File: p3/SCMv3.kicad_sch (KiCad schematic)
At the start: 122 parts, among them IC1 40106, IC2 40106, IC3 TL082, J1 ISP, J1-OUT8 JACK-MONO-SWB, J2 Conn_01x02, J2-OUT7 JACK-MONO-SWB, J3 POWER, J3-OUT6 JACK-MONO-SWB, J4-OUT5 JACK-MONO-SWB, J5-OUT4 JACK-MONO-SWB, J6-OUT3 JACK-MONO-SWB, J7-OUT2 JACK-MONO-SWB, J8-OUT1 JACK-MONO-SWB, J9-CLK_IN1 JCLK_IN, Q1 Si2318, Q2 Si2318, Q3 Si2318, Q4 Si2318, U1 ATMEGA328-AU, Y1 16MHz_18pF_FA238

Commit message: p3 ready to connect pins: then route
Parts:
- removed J1: ISP, 4ms_Connector:Pins_2x03_2.54mm_TH, symbol 4ms_Connector:Conn_02x03
- removed U1: ATMEGA328-AU, 4ms_Package_QFP:TQFP-32_7x7mm_P0.8mm, symbol 4ms_IC:ATMEGA328-AU
- added C18, C22, C23: 0.1uF_0603_16V, 4ms_Capacitor:C_0603, symbol 4ms_Capacitor:0.1uF_0603_16V
- added C21: 10uF_0603_10V, 4ms_Capacitor:C_0603, symbol 4ms_Capacitor:10uF_0603_10V
- added J1: Conn_01x06, 4ms_Connector:Pins_1x06_2.54mm_TH_SWD, symbol 4ms_Connector:Conn_01x06
- added U2: AP7384-33, 4ms_Package_SOT:SOT23-3_PO132, symbol 4ms_Regulator:AP7384-33
- gave numbers to parts that had none: 2
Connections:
- net +12V: now also C18.1, C22.1, C23.1, U2.1 (VI)
- net +3.3VA: now also C21.1, U2.2 (VO)
- net +3V3: now also R16.2, J1.1 (Pin_1)
- net +5V: no longer C15.1, R16.2
- net -12VA: now also C15.1
- net GND: now also C18.2, C21.2, C22.2, C23.2, J1.3 (Pin_3), U2.3 (GND)
- net RESET: now also U1.4 (NRST), J1.5 (Pin_5)
- net CLKBUS_PWRHDR: now reaches J2.2 (Pin_2), J3.1 (P1), J3.2 (P2)
- net at C5.1, Y1.2: now also U1.2 (PF0)
- net at C4.1, Y1.1: now also U1.3 (PF1)
- net SWDIO: now reaches U1.23 (PA13)
- net SWDIO: now also J1.4 (Pin_4)
- net SWCLK: now reaches U1.24 (PA14)
- net SWCLK: now also J1.2 (Pin_2)
- net UC_OUT4_MOSI renamed UC_OUT4
- net UC_OUT5_MISO renamed UC_OUT5
- net UC_OUT6_SCK renamed UC_OUT6
- no-connect marks 43 -> 40
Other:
- note added: "ADC"
- note added: "CLKBUS->IN Jumper"
- note added: "Connect to an ADC pin:"
- note added: "Connect to any available pin:"
- note added: "FREERUN Jumper"
- note added: "LED Brightness Trimpot"
- moved on the sheet: C12, C13, C14, C16, C17, C19, C20, C4, C5, D10, D11, IC1G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

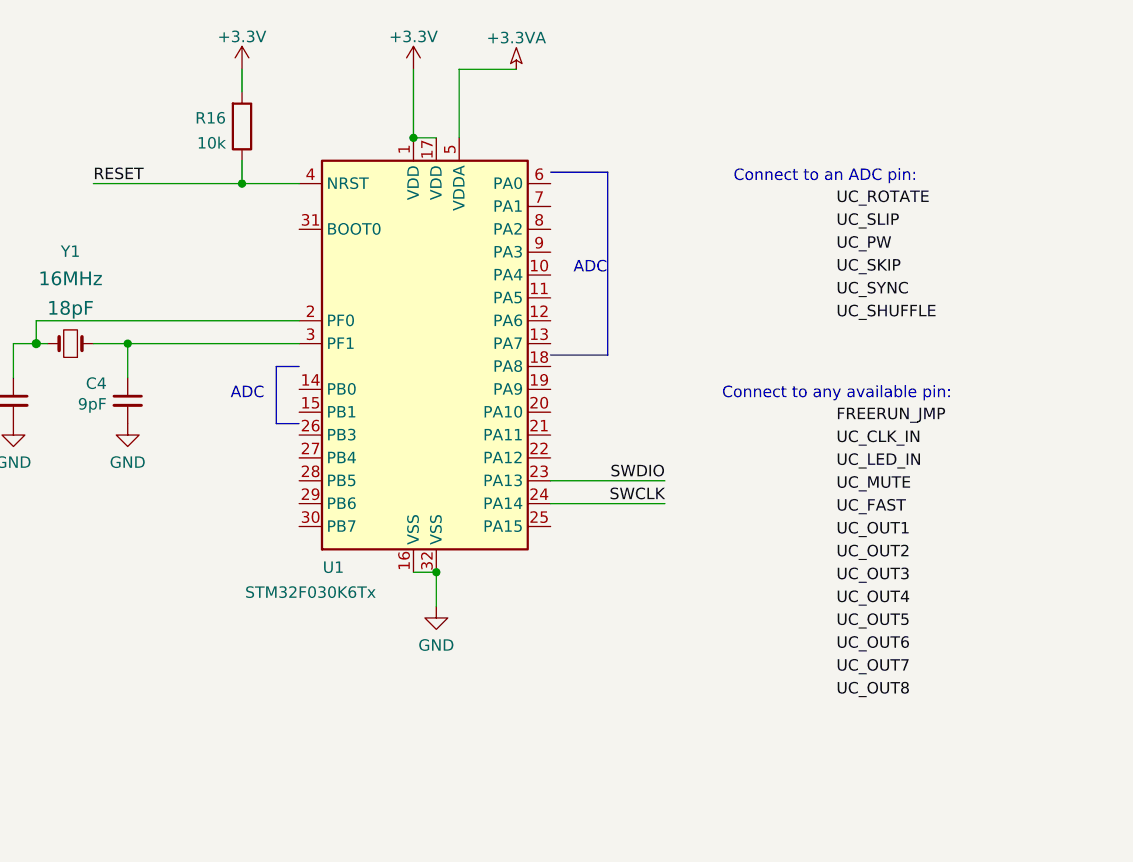
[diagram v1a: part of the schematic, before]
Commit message: Atmega replacement and other mods
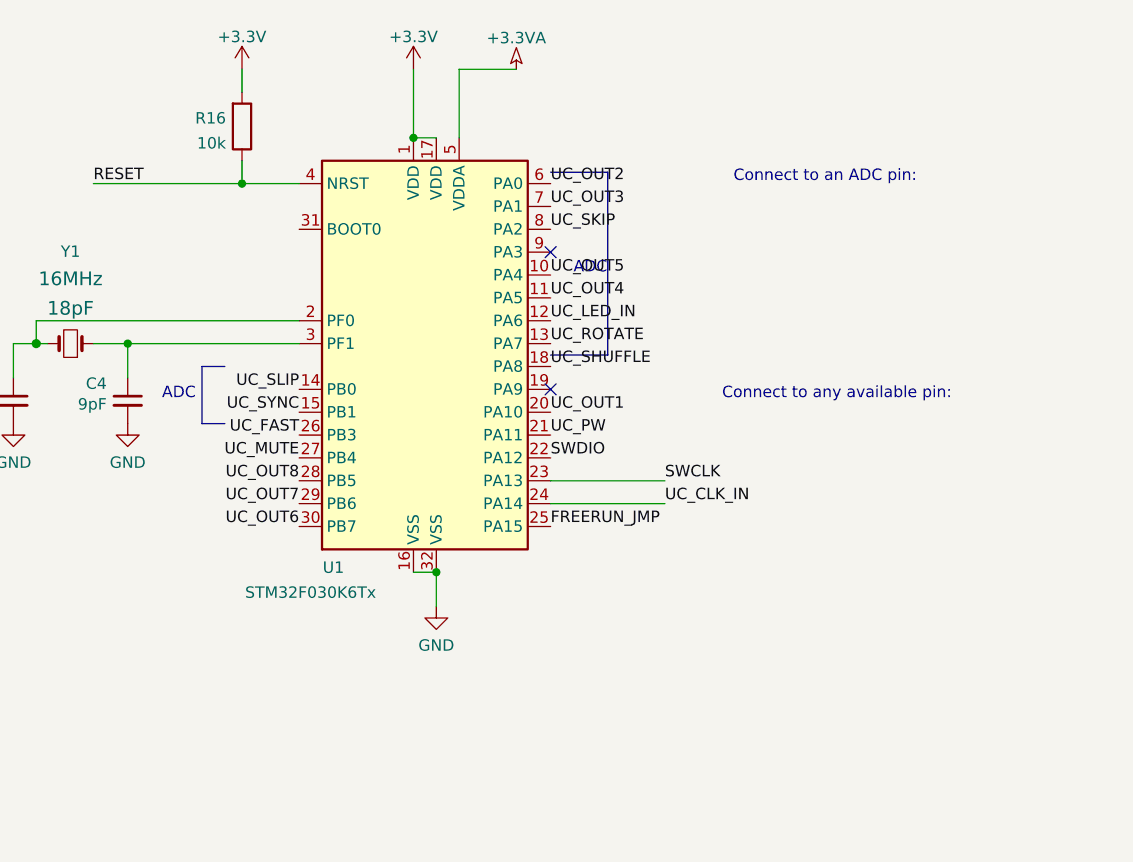
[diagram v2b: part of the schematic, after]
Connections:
- net FREERUN_JMP: now also U1.25 (PA15)
- net SWCLK: now also U1.23 (PA13); no longer U1.24 (PA14)
- net SWDIO: now also U1.22 (PA12); no longer U1.23 (PA13)
- net UC_CLK_IN: now also U1.24 (PA14)
- net UC_FAST: now also U1.26 (PB3)
- net UC_LED_IN: now also U1.12 (PA6)
- net UC_MUTE: now also U1.27 (PB4)
- net UC_OUT1: now also U1.20 (PA10)
- net UC_OUT2: now also U1.6 (PA0)
- net UC_OUT3: now also U1.7 (PA1)
- net UC_OUT4: now also U1.11 (PA5)
- net UC_OUT5: now also U1.10 (PA4)
- net UC_OUT6: now also U1.30 (PB7)
- net UC_OUT7: now also U1.29 (PB6)
- net UC_OUT8: now also U1.28 (PB5)
- net UC_PW: now also U1.21 (PA11)
- net UC_ROTATE: now also U1.13 (PA7)
- net UC_SHUFFLE: now also U1.18 (PA8)
- net UC_SKIP: now also U1.8 (PA2)
- net UC_SLIP: now also U1.14 (PB0)
- net UC_SYNC: now also U1.15 (PB1)
- no-connect marks 40 -> 42
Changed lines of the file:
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@@
   (no_connect (at 44.45 353.06))
   (no_connect (at 63.5 44.45))
+  (no_connect (at 91.44 111.76))
+  (no_connect (at 91.44 127))
   (no_connect (at 185.42 49.53))
   (no_connect (at 185.42 54.61))
@@
     (stroke (width 0) (type solid) (color 0 0 0 0))
   )
-  (polyline (pts (xy 60.96 124.46) (xy 60.96 130.81))
-    (stroke (width 0) (type default) (color 0 0 0 0))
-  )
-  (polyline (pts (xy 60.96 130.81) (xy 63.5 130.81))
-    (stroke (width 0) (type default) (color 0 0 0 0))
-  )
-  (polyline (pts (xy 63.5 124.46) (xy 60.96 124.46))
+  (polyline (pts (xy 52.705 124.46) (xy 52.705 130.81))
+    (stroke (width 0) (type default) (color 0 0 0 0))
+  )
+  (polyline (pts (xy 52.705 130.81) (xy 55.245 130.81))
+    (stroke (width 0) (type default) (color 0 0 0 0))
+  )
+  (polyline (pts (xy 55.245 124.46) (xy 52.705 124.46))
     (stroke (width 0) (type default) (color 0 0 0 0))
   )
@@
     (effects (font (size 2.54 2.54)) (justify left bottom))
   )
+  (text "ADC" (at 48.26 128.27 0)
+    (effects (font (size 1.27 1.27)) (justify left bottom))
+  )
   (text "FREERUN Jumper" (at 53.34 256.54 0)
     (effects (font (size 2.54 2.54)) (justify left bottom))
   )
-  (text "ADC" (at 55.88 128.27 0)
-    (effects (font (size 1.27 1.27)) (justify left bottom))
-  )
   (text "ADC" (at 93.98 114.3 0)
     (effects (font (size 1.27 1.27)) (justify left bottom))
@@
     (effects (font (size 1.27 1.27)) (justify left bottom))
   )
+  (label "UC_SLIP" (at 63.5 127 180)
+    (effects (font (size 1.27 1.27)) (justify right bottom))
+  )
+  (label "UC_SYNC" (at 63.5 129.54 180)
+    (effects (font (size 1.27 1.27)) (justify right bottom))
+  )
+  (label "UC_FAST" (at 63.5 132.08 180)
+    (effects (font (size 1.27 1.27)) (justify right bottom))
+  )
+  (label "UC_MUTE" (at 63.5 134.62 180)
+    (effects (font (size 1.27 1.27)) (justify right bottom))
+  )
+  (label "UC_OUT8" (at 63.5 137.16 180)
+    (effects (font (size 1.27 1.27)) (justify right bottom))
+  )
+  (label "UC_OUT7" (at 63.5 139.7 180)
+    (effects (font (size 1.27 1.27)) (justify right bottom))
+  )
+  (label "UC_OUT6" (at 63.5 142.24 180)
+    (effects (font (size 1.27 1.27)) (justify right bottom))
+  )
   (label "FREERUN_JMP" (at 64.77 264.16 180)
     (effects (font (size 1.27 1.27)) (justify right bottom))
   )
-  (label "SWDIO" (at 104.14 137.16 180)
-    (effects (font (size 1.27 1.27)) (justify right bottom))
-  )
-  (label "SWCLK" (at 104.14 139.7 180)
-    (effects (font (size 1.27 1.27)) (justify right bottom))
+  (label "UC_OUT2" (at 91.44 104.14 0)
+    (effects (font (size 1.27 1.27)) (justify left bottom))
+  )
+  (label "UC_OUT3" (at 91.44 106.68 0)
+    (effects (font (size 1.27 1.27)) (justify left bottom))
+  )
+  (label "UC_SKIP" (at 91.44 109.22 0)
+    (effects (font (size 1.27 1.27)) (justify left bottom))
+  )
+  (label "UC_OUT5" (at 91.44 114.3 0)
+    (effects (font (size 1.27 1.27)) (justify left bottom))
+  )
+  (label "UC_OUT4" (at 91.44 116.84 0)
+    (effects (font (size 1.27 1.27)) (justify left bottom))
+  )
+  (label "UC_LED_IN" (at 91.44 119.38 0)
+    (effects (font (size 1.27 1.27)) (justify left bottom))
+  )
+  (label "UC_ROTATE" (at 91.44 121.92 0)
+    (effects (font (size 1.27 1.27)) (justify left bottom))
+  )
+  (label "UC_SHUFFLE" (at 91.44 124.46 0)
+    (effects (font (size 1.27 1.27)) (justify left bottom))
+  )
+  (label "UC_OUT1" (at 91.44 129.54 0)
+    (effects (font (size 1.27 1.27)) (justify left bottom))
+  )
+  (label "UC_PW" (at 91.44 132.08 0)
+    (effects (font (size 1.27 1.27)) (justify left bottom))
+  )
+  (label "SWDIO" (at 91.44 134.62 0)
+    (effects (font (size 1.27 1.27)) (justify left bottom))
+  )
+  (label "FREERUN_JMP" (at 91.44 142.24 0)
+    (effects (font (size 1.27 1.27)) (justify left bottom))
+  )
+  (label "SWCLK" (at 104.14 137.16 0)
+    (effects (font (size 1.27 1.27)) (justify left bottom))
+  )
+  (label "UC_CLK_IN" (at 104.14 139.7 0)
+    (effects (font (size 1.27 1.27)) (justify left bottom))
   )
   (label "IN-SW" (at 104.14 213.36 0)
     (effects (font (size 1.27 1.27)) (justify left bottom))
   )
-  (label "UC_ROTATE" (at 123.19 106.68 0)
-    (effects (font (size 1.27 1.27)) (justify left bottom))
-  )
-  (label "UC_SLIP" (at 123.19 109.22 0)
-    (effects (font (size 1.27 1.27)) (justify left bottom))
-  )
-  (label "UC_PW" (at 123.19 111.76 0)
-    (effects (font (size 1.27 1.27)) (justify left bottom))
-  )
-  (label "UC_SKIP" (at 123.19 114.3 0)
-    (effects (font (size 1.27 1.27)) (justify left bottom))
-  )
-  (label "UC_SYNC" (at 123.19 116.84 0)
-    (effects (font (size 1.27 1.27)) (justify left bottom))
-  )
-  (label "UC_SHUFFLE" (at 123.19 119.38 0)
-    (effects (font (size 1.27 1.27)) (justify left bottom))
-  )
-  (label "FREERUN_JMP" (at 123.19 130.81 0)
-    (effects (font (size 1.27 1.27)) (justify left bottom))
-  )
-  (label "UC_CLK_IN" (at 123.19 133.35 0)
-    (effects (font (size 1.27 1.27)) (justify left bottom))
-  )
-  (label "UC_LED_IN" (at 123.19 135.89 0)
-    (effects (font (size 1.27 1.27)) (justify left bottom))
-  )
-  (label "UC_MUTE" (at 123.19 138.43 0)
-    (effects (font (size 1.27 1.27)) (justify left bottom))
-  )
-  (label "UC_FAST" (at 123.19 140.97 0)
-    (effects (font (size 1.27 1.27)) (justify left bottom))
-  )
-  (label "UC_OUT1" (at 123.19 143.51 0)
-    (effects (font (size 1.27 1.27)) (justify left bottom))
-  )
-  (label "UC_OUT2" (at 123.19 146.05 0)
-    (effects (font (size 1.27 1.27)) (justify left bottom))
-  )
-  (label "UC_OUT3" (at 123.19 148.59 0)
-    (effects (font (size 1.27 1.27)) (justify left bottom))
-  )
-  (label "UC_OUT4" (at 123.19 151.13 0)
-    (effects (font (size 1.27 1.27)) (justify left bottom))
-  )
-  (label "UC_OUT5" (at 123.19 153.67 0)
-    (effects (font (size 1.27 1.27)) (justify left bottom))
-  )
-  (label "UC_OUT6" (at 123.19 156.21 0)
-    (effects (font (size 1.27 1.27)) (justify left bottom))
-  )
-  (label "UC_OUT7" (at 123.19 158.75 0)
-    (effects (font (size 1.27 1.27)) (justify left bottom))
-  )
-  (label "UC_OUT8" (at 123.19 161.29 0)
-    (effects (font (size 1.27 1.27)) (justify left bottom))
-  )

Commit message: Notes on schematic about wrong pin assignments. Cleaned up schematic, too
To Do:
Sch: Some nets requiring an ADC pin are connected to non-ADC pins.
PCB:  Fix routing to pots with V+/GND swapped on pins 1/3. Also fix routing to ADC pins

Done:
Removed R16 (RESET->V+) and replaced with C24 (RESET->GND).
Connected BOOT0 to GND.
Flipped V+/GND on three pots that were backwards on last proto (fixed on schematic only)
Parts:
- removed R16: 10k_0603, 4ms_Resistor:R_0603, symbol 4ms_Resistor:10k_0603
- added C24: 0.1uF_0603_16V, 4ms_Capacitor:C_0603, symbol 4ms_Capacitor:0.1uF_0603_16V
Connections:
- net +5V: now also PPW1.3 (Right), PSHUFFLE1.3 (Right), PSKIP1.3 (Right); no longer PPW1.1 (Left), PSHUFFLE1.1 (Left), PSKIP1.1 (Left)
- net GND: now also PPW1.1 (Left), PSHUFFLE1.1 (Left), PSKIP1.1 (Left), U1.31 (BOOT0), C24.2; no longer PPW1.3 (Right), PSHUFFLE1.3 (Right), PSKIP1.3 (Right)
- net RESET: now also C24.1
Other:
- note added: "Buttons/Gate Jacks"
- note added: "Connect to an ADC pin: FIX: -UC_SHUFFLE must connect to an ADC pin -UC_PW must connect to an ADC pin Note: UC_ROTATE, UC_SKIP, UC_SLIP are already correctly connected to ADC pins, make sure they must remain so when you re-route Note: Valid ADC pins are: PA0, PA1, PA2, PA3, PA4, PA5, PA6, PA7 PB0, PB1 Note: -UC_OUTs, UC_LED_IN, UC_SYNC are connected to ADC pins. If you want, they can be moved to n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"
- note added: "LEDs"
- note added: "Microcontroller"
- note added: "Outputs"
- note added: "POWER"
- note added: "Pots/CV Jacks"
- note added: "SWD programming header"
- note added: "Trig Jacks"
- note added: "Unused gates"
- note removed: "Connect to an ADC pin:"
- note removed: "Connect to any available pin:"
- moved on the sheet: BFAST1, BMUTE1, C1, C10, C11, C12, C14, C16, C17, C18, C19, C2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

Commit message: Fixed errors in pcb and updated schematic accordingly
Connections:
- net UC_PW: now also U1.9 (PA3); no longer U1.21 (PA11)
- net UC_SHUFFLE: now also U1.15 (PB1); no longer U1.18 (PA8)
- net UC_SYNC: now also U1.19 (PA9); no longer U1.15 (PB1)
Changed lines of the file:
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@@
   (no_connect (at 44.45 353.06))
   (no_connect (at 63.5 50.8))
-  (no_connect (at 91.44 111.76))
-  (no_connect (at 91.44 127))
+  (no_connect (at 91.44 124.46))
+  (no_connect (at 91.44 132.08))
   (no_connect (at 186.69 80.01))
   (no_connect (at 186.69 85.09))
@@
     (effects (font (size 1.27 1.27)) (justify right bottom))
   )
-  (label "UC_SYNC" (at 63.5 129.54 180)
+  (label "UC_SHUFFLE" (at 63.5 129.54 180)
     (effects (font (size 1.27 1.27)) (justify right bottom))
   )
@@
     (effects (font (size 1.27 1.27)) (justify left bottom))
   )
+  (label "UC_PW" (at 91.44 111.76 0)
+    (effects (font (size 1.27 1.27)) (justify left bottom))
+  )
   (label "UC_OUT5" (at 91.44 114.3 0)
     (effects (font (size 1.27 1.27)) (justify left bottom))
@@
     (effects (font (size 1.27 1.27)) (justify left bottom))
   )
-  (label "UC_SHUFFLE" (at 91.44 124.46 0)
+  (label "UC_SYNC" (at 91.44 127 0)
     (effects (font (size 1.27 1.27)) (justify left bottom))
   )
@@
     (effects (font (size 1.27 1.27)) (justify left bottom))
   )
-  (label "UC_PW" (at 91.44 132.08 0)
-    (effects (font (size 1.27 1.27)) (justify left bottom))
-  )
